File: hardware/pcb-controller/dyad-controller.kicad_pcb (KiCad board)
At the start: 2 copper layers, 35 x 50 mm, 45 parts, among them J1 USB_C_Receptacle_USB2.0, J10 USB-C split link, J2 SWD, J6 HC-FPC-0.5-20P-FH20, J7 HC-FPC-0.5-20P-FH20, J8 HC-FPC-0.5-14P-FH20, J9 USB-C split link, SW1 BOOTSEL, SW2 RESET, U1 W25Q128JVS, U2 USBLC6-2SC6, U3 RP2040, U4 XC6206PxxxMR-Regulator_Linear, Y1 12MHz

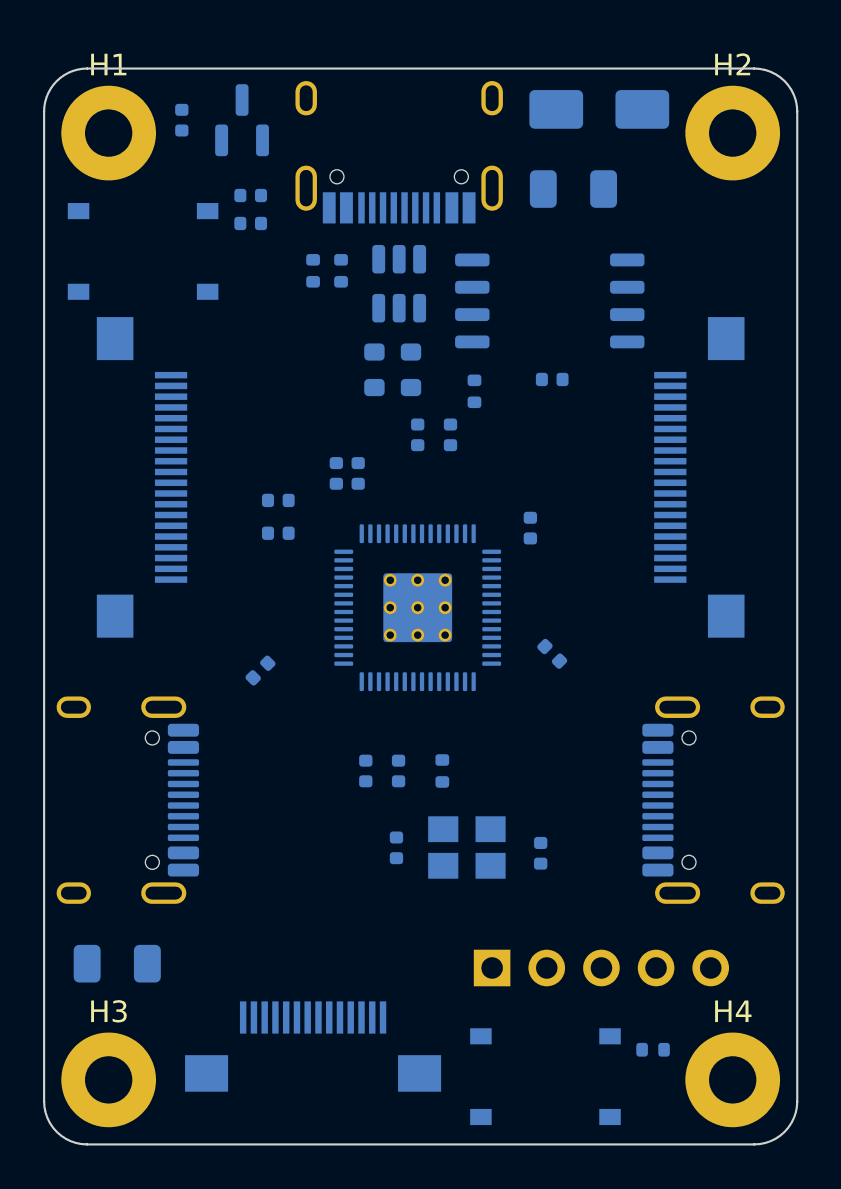
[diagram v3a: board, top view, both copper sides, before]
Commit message: Route the controller with Freerouting and make it DRC-clean
Net classes: Power (VBUS, VBUS_FUSED, +5V, VBUS_SPLIT) at 0.4 mm -- the
widest track that still enters the 0.5 mm-pitch FFC power pads -- and
everything else at 0.2 mm, both 0.15 mm clearance. The upstream Power class
also held +3V3, +1V1 and GND at 0.381 mm, which cannot reach the RP2040's
0.4 mm-pitch pads; those nets now use Default, and GND gets a fill later.
No USB differential-pair class: at 12 Mbps full speed the impedance is moot.

Routed with Freerouting 2.4.1 headless via KiCad's own DSN/SES path (the
Konnect exporter accepts only front-side parts and straight outlines). The
optimizer is off: one pass took 14 minutes and the output is written only
at the end. Result: all 187 nets, 115 vias, 1,050 mm on F.Cu, 952 mm on B.Cu.

Design rules, to accept what was routed without loosening it board-wide:
- min track width 0.2 -> 0.15 mm, covering Freerouting's 53 neck-downs.
- dyad-controller.kicad_dru: 0.13 mm clearance for copper touching J1's
  pads only, whose 0.2 mm gaps make 0.15 impossible at the pads.
- min copper-to-edge clearance 0.0 -> 0.3 mm, so DRC checks it at all;
  that gap is how J2's pin past the board edge went unflagged earlier.

Freerouting does not model hole-to-hole spacing: six vias sat 0.44-0.496
mm from a neighbouring hole against the 0.5 mm rule. Each moved 0-0.07 mm
to the nearest spot clearing every hole and all other-net copper on both
layers, dragging its tracks along; for the SD0/+1V1 pair the +1V1 via moved,
as SD0 had no clean spot within 0.35 mm.

DRC: 0 errors, 0 unconnected. 78 warnings (silkscreen, library versions).
Parity: 14 field-copy differences.

Co-Authored-By: Claude Opus 5.5 <noreply@anthropic.com>
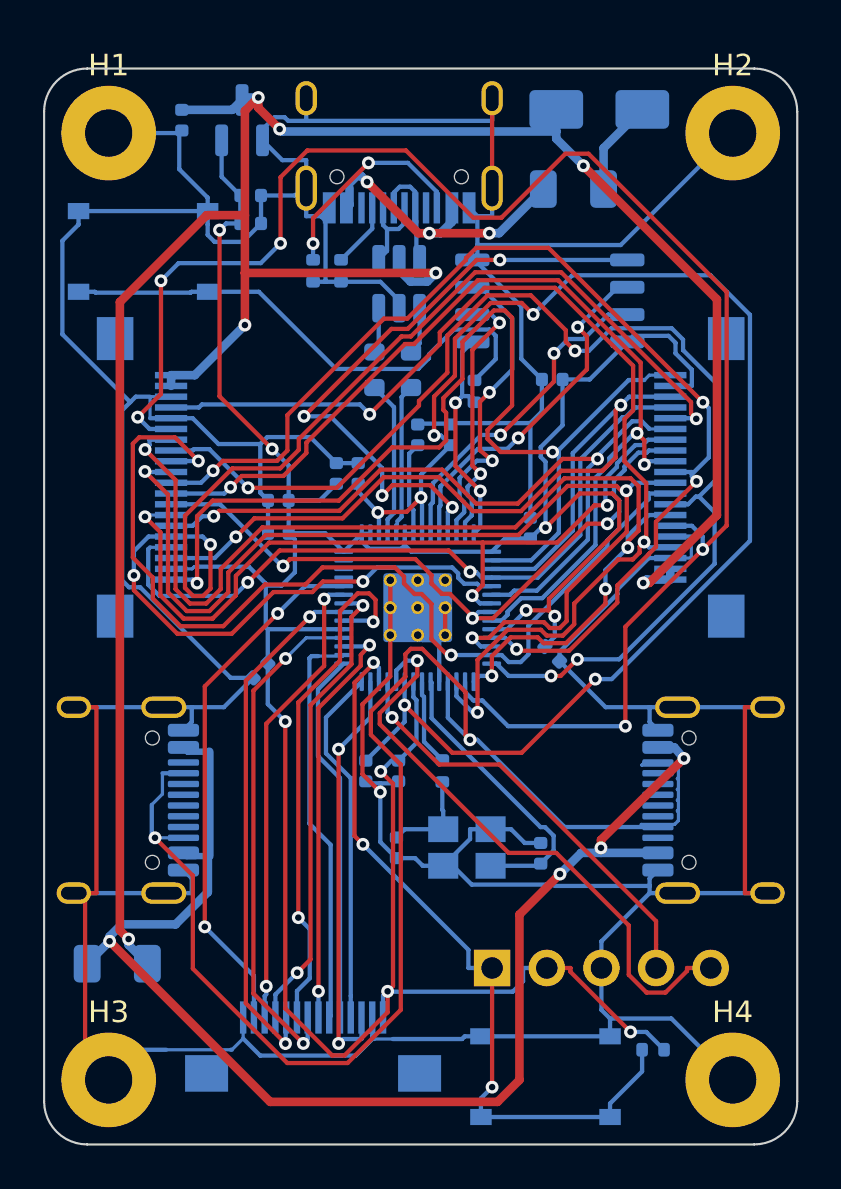
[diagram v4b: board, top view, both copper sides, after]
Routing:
- net GND: track 0.00 -> 297.4 mm, vias 0 -> 1
- net +3V3: track 0.00 -> 147.2 mm, vias 0 -> 9
- net +5V: track 0.00 -> 113.0 mm, vias 0 -> 7
- net /GPIO13: track 0.00 -> 77.4 mm, vias 0 -> 5
- net /GPIO15: track 0.00 -> 70.1 mm, vias 0 -> 2
- net +1V1: track 0.00 -> 67.7 mm, vias 0 -> 6
- net /GPIO3: track 0.00 -> 65.0 mm, vias 0 -> 4
- net /VBUS_SPLIT: track 0.00 -> 61.5 mm, vias 0 -> 4
- net /GPIO11: track 0.00 -> 57.4 mm, vias 0 -> 4
- net /GPIO8: track 0.00 -> 52.7 mm, vias 0 -> 4
- net /GPIO14: track 0.00 -> 51.5 mm, vias 0 -> 3
- net /GPIO12: track 0.00 -> 50.9 mm, vias 0 -> 4
- net /GPIO0: track 0.00 -> 49.3 mm, vias 0 -> 2
- net /GPIO9: track 0.00 -> 47.4 mm, vias 0 -> 3
- net /GPIO7: track 0.00 -> 46.4 mm, vias 0 -> 3
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
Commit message: Add GND fills on both layers with stitching vias
A GND zone on F.Cu and B.Cu covering the whole outline: 0.2 mm clearance,
thermal-relief pads, unconnectable islands removed. 72 stitching vias on a
2 mm minimum pitch wherever both layers' fill has room for one, outside
part courtyards and at least 0.5 mm from every other hole.

U3's exposed pad (pad 57 and its 9 vias) and TESTEN (pin 19) connect solid
rather than through thermal relief: the fan-out tracks starved their spokes,
and the exposed pad is the RP2040's ground and heat path anyway.

Result: F.Cu 42% covered in 8 pieces (largest 591 mm^2), B.Cu 50% in 10
(largest 785 mm^2). The matrix bundle running across F.Cu is what breaks
that layer's fill up between U3, J1 and the flash -- the trade-off to weigh
against routing the bundle on B.Cu instead.

DRC: 0 errors, 0 unconnected. Parity: 14 field-copy differences.

Co-Authored-By: Claude Opus 5.5 <noreply@anthropic.com>
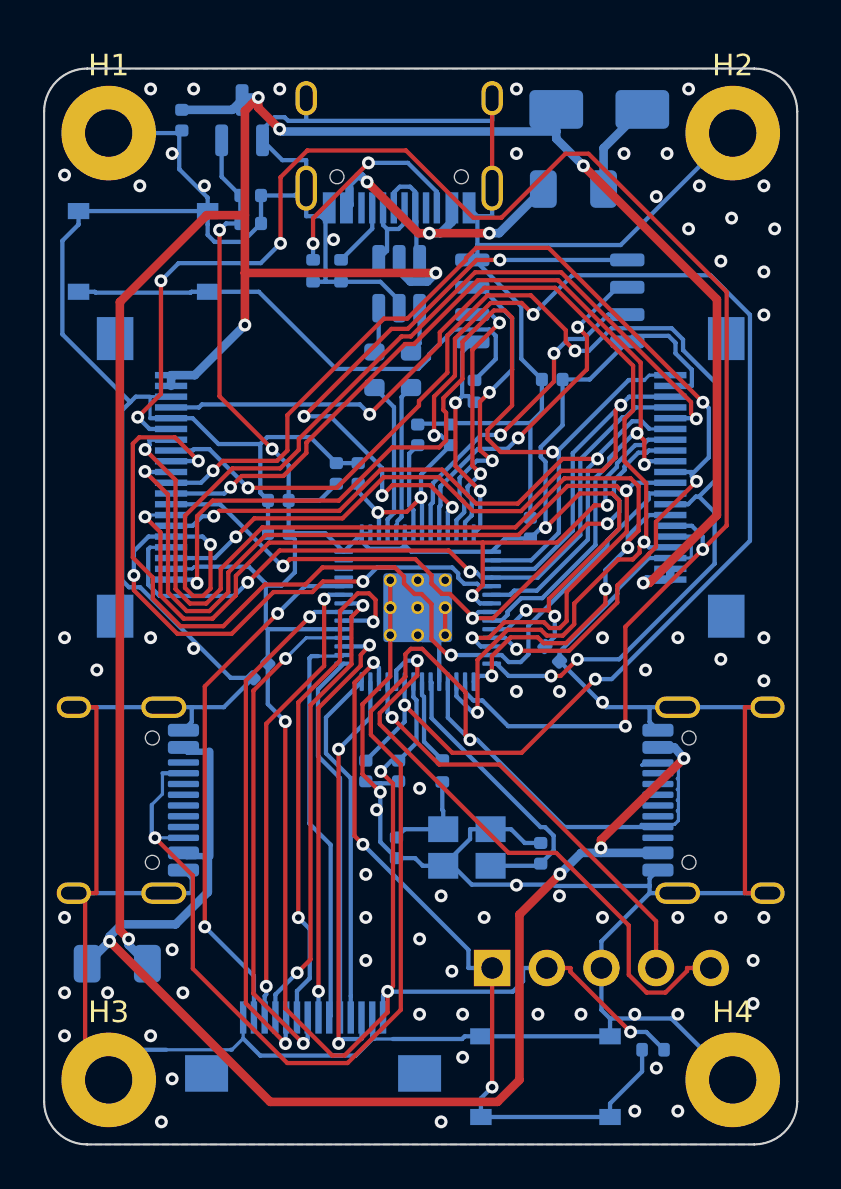
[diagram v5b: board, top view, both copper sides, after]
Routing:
- net GND: vias 1 -> 73
- added copper zone on B.Cu, net GND
- added copper zone on F.Cu, net GND

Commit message: Move the flash next to the RP2040 and reroute the controller
QSPI is the board's fastest bus (XIP at ~66 MHz), yet with U1 ~10 mm away
behind the USB column its six lines totalled ~99 mm, only 12% of it over
ground. Changing Freerouting's layer costs alone could not fix that; the
placement could.

Placement: U1 moved directly behind U3's QSPI side to (207.3, 61.4),
turned 180 degrees -- straight-line QSPI length 73.9 -> 42.6 mm. C1 now
sits at U1's supply pin, R1 at its CS pin, and C5 moved 3 mm left, still
between the two +1V1 pins it serves.

Routing: all copper cleared and rerouted. Of four Freerouting runs on this
placement, default costs with random item selection was the only one that
both routed 100% and kept ground under the fast nets; F.Cu-favouring costs
gave the most continuous F.Cu fill but left QSPI over almost none.

Clean-up, as for the previous routing: 11 vias moved 0-0.36 mm to meet
0.5 mm hole spacing; ~3.9 mm of VBUS and a D- stub at J1's fine-pitch pads
necked to 0.25 / 0.18 mm for clearance; GND fills on both layers with 71
stitching vias; U3's exposed pad and TESTEN plus 8 fine-pitch GND pads
(J7, J8, J10 shell, U1) connect solid, as thermal spokes do not fit.

Against a7200b8: QSPI 98.6 -> 52.0 mm of track with 12% -> 26% over
ground; crystal 27% -> 42%. USB is the trade: 28 -> 44 mm, 15% -> 4%,
acceptable at 12 Mbps. F.Cu fill 42% -> 48%; B.Cu 50% -> 46%.

DRC: 0 errors, 0 unconnected. Parity: 14 field-copy differences.

Co-Authored-By: Claude Opus 5.5 <noreply@anthropic.com>
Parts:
- moved R1 7.37 mm to (210.9, 57.4)
- moved U1 5.60 mm to (207.3, 61.4), turned to 180 degrees
- moved C1 3.88 mm to (204.2, 57.6)
- moved C5 2.99 mm to (199.9, 62.0)
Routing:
- net +1V1: track 67.7 -> 23.7 mm, vias 6 -> 3
- net /GPIO12: track 50.9 -> 86.8 mm, vias 4 -> 5
- net GND: track 297.4 -> 330.2 mm, vias 73 -> 76
- net /GPIO10: track 45.5 -> 75.6 mm, vias 2 -> 7
- net /GPIO8: track 52.7 -> 81.2 mm, vias 4 -> 3
- net SD0: track 29.1 -> 3.70 mm, vias 4 -> 0
- net /GPIO7: track 46.4 -> 70.3 mm, vias 3 -> 5
- net /GPIO6: track 31.5 -> 54.2 mm, vias 3 -> 2
- net /GPIO14: track 51.5 -> 72.1 mm, vias 3 -> 6
- net /GPIO4: track 36.2 -> 54.4 mm, vias 2 -> 3
- net +5V: track 113.0 -> 97.0 mm, vias 7 -> 6
- net /GPIO2: track 34.0 -> 49.7 mm
- net QSPI_CLK: track 16.5 -> 5.20 mm, vias 2 -> 0
- net /GPIO13: track 77.4 -> 66.2 mm, vias 5 -> 2
- net D_USB_N: track 4.26 -> 15.2 mm, vias 0 -> 2
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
